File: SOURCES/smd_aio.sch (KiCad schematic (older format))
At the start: 43 parts, among them P2 CONN_01X03, P3 CONN_02X05, Q1 BSS123, Q2 BSS123, Q3 BSS123, Q4 BSS123, Q5 FZT751TA, SW1 SW_PUSH, U2 24AA256SN

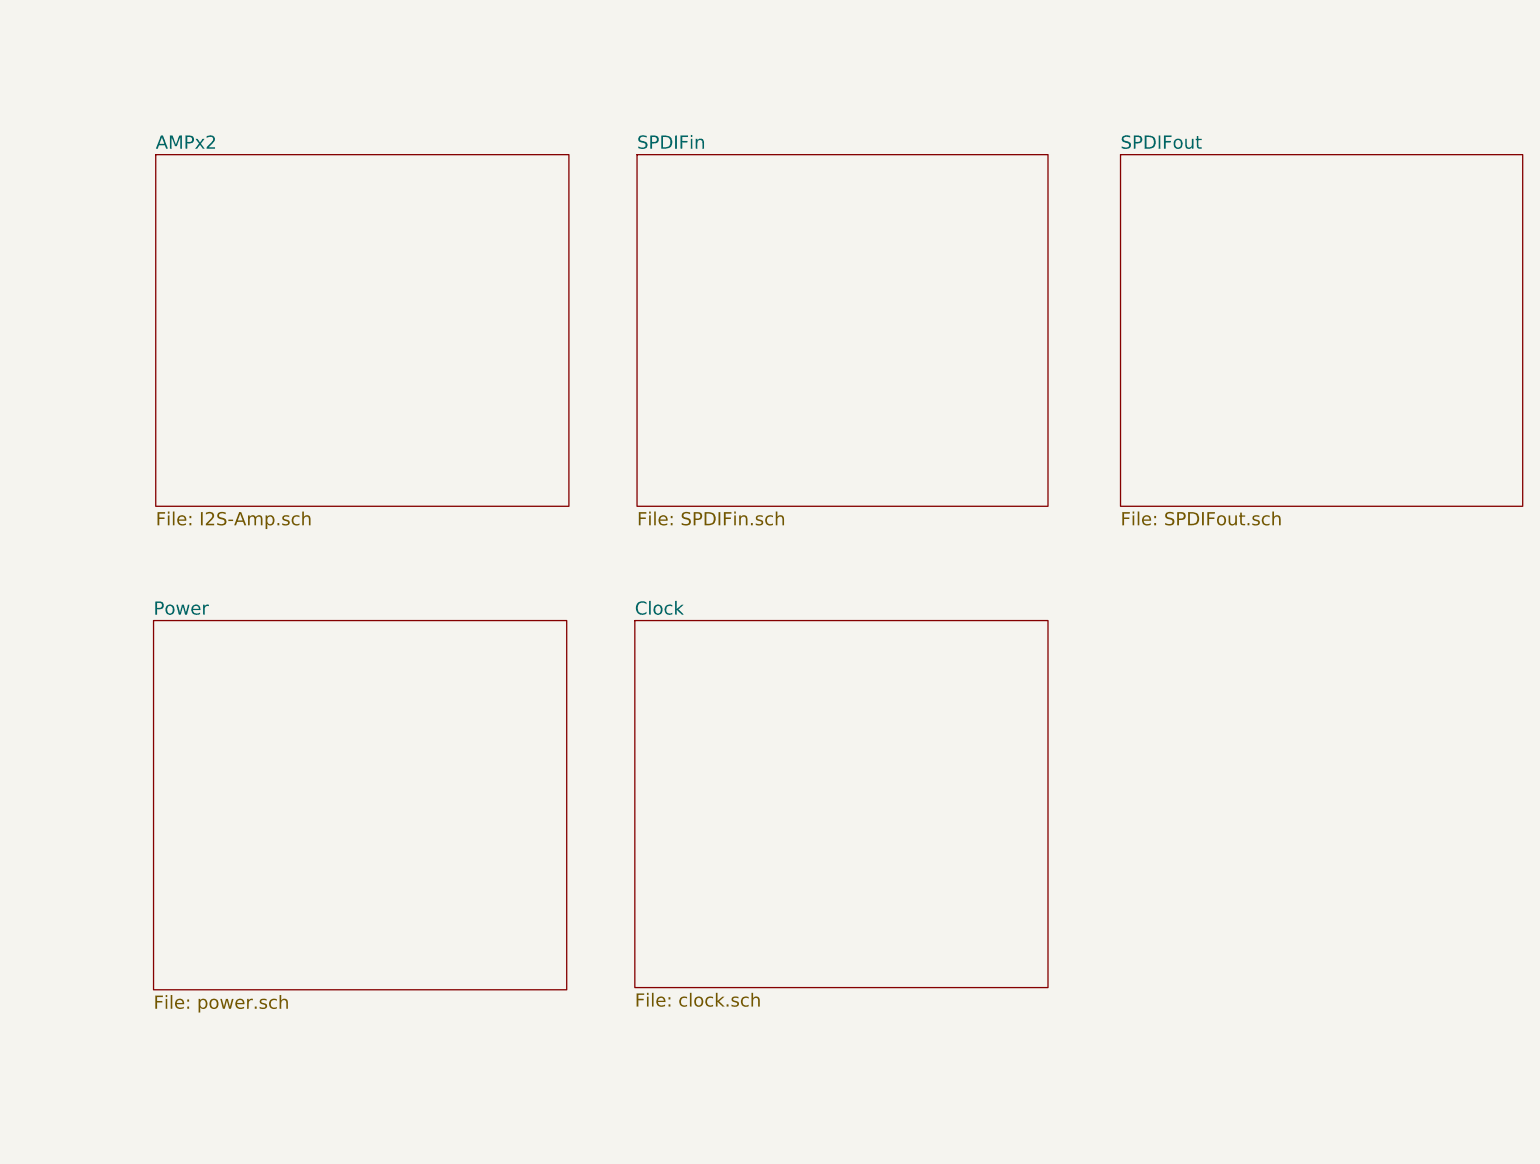
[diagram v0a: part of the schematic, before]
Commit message: adding AMPx2 done
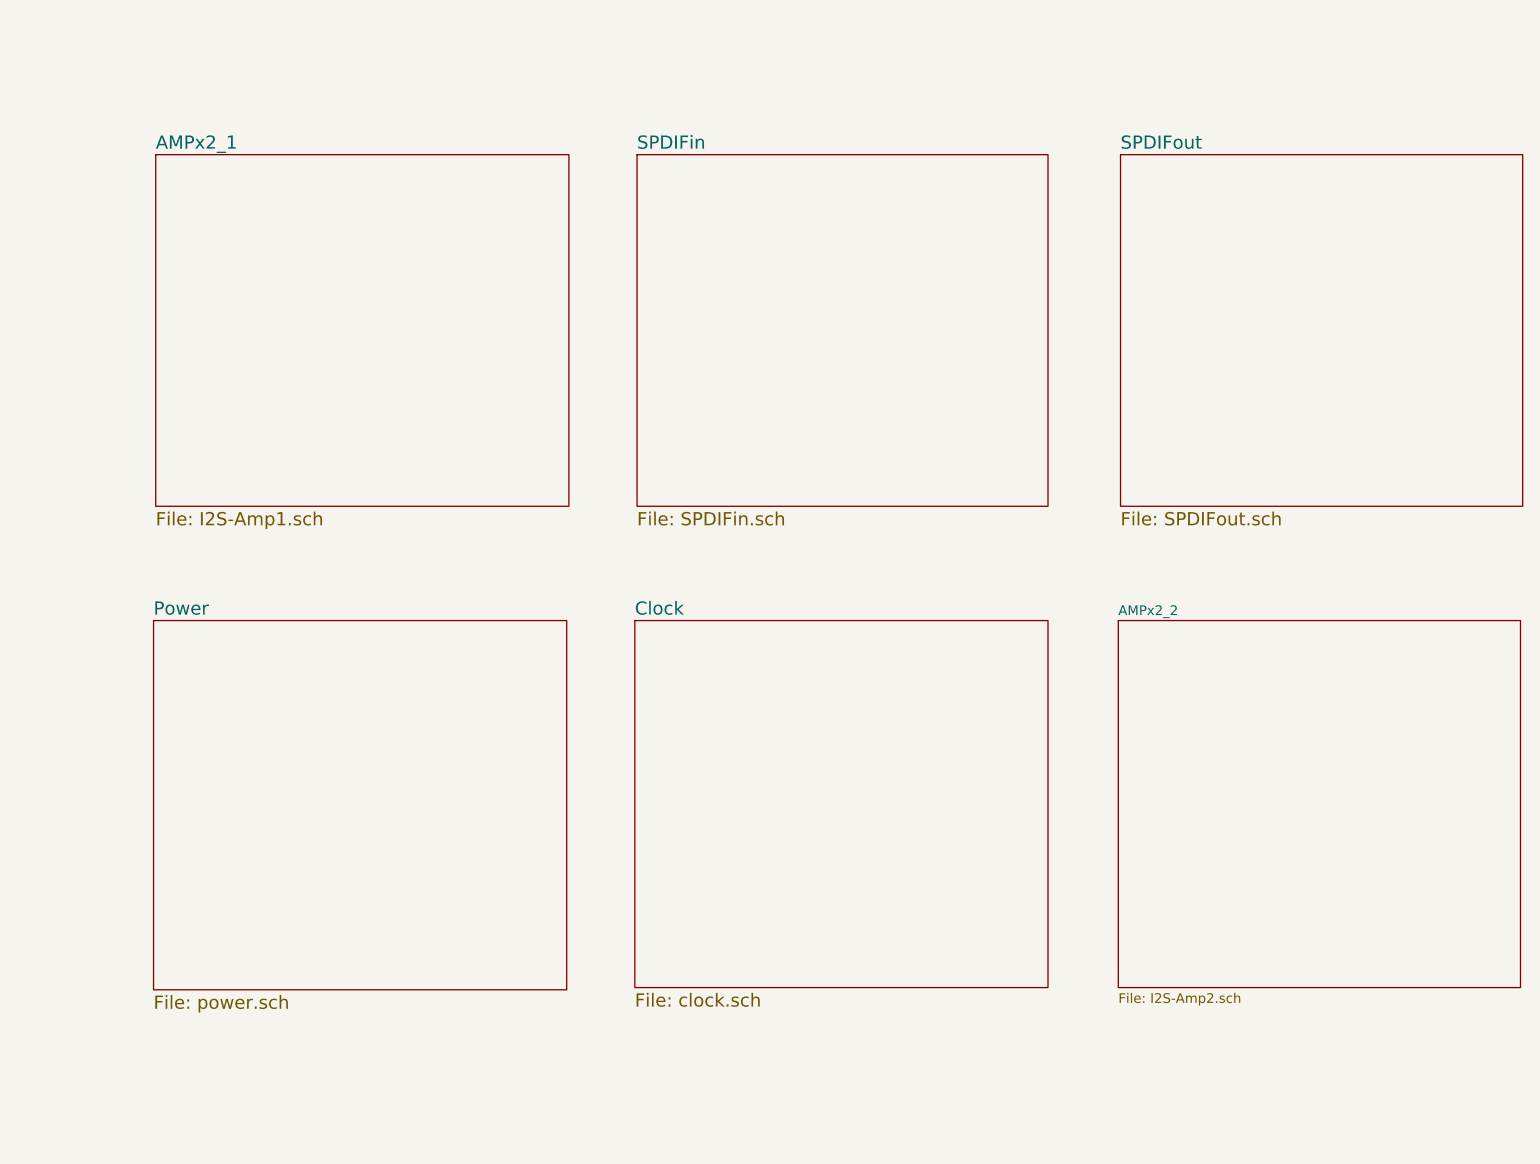
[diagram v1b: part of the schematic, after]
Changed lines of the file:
@@
 $Descr A3 16535 11693
 encoding utf-8
-Sheet 1 6
+Sheet 1 7
 Title ""
 Date ""
@@
 S 9380 1320 1880 1600
 U 5AF9FF80
-F0 "AMPx2" 60
-F1 "I2S-Amp.sch" 60
+F0 "AMPx2_1" 60
+F1 "I2S-Amp1.sch" 60
 $EndSheet
 $Sheet
@@
 F1 "clock.sch" 60
 $EndSheet
+$Sheet
+S 13760 3440 1830 1670
+U 5B04B659
+F0 "AMPx2_2" 44
+F1 "I2S-Amp2.sch" 44
+$EndSheet
 $EndSCHEMATC

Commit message: rearranged sheets
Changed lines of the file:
@@
 	4010 4540 4010 4465
 Wire Wire Line
-	3370 4540 4380 4540
+	3370 4540 3520 4540
+Wire Wire Line
+	3520 4540 3670 4540
+Wire Wire Line
+	3670 4540 3810 4540
+Wire Wire Line
+	3810 4540 4010 4540
+Wire Wire Line
+	4010 4540 4160 4540
+Wire Wire Line
+	4160 4540 4380 4540
 Wire Wire Line
 	3370 4470 3370 4540
@@
 	2720 4300 2720 4210
 Wire Wire Line
-	1440 3900 1440 4250
-Wire Wire Line
-	1420 4110 2720 4110
+	1440 3900 1440 4110
+Wire Wire Line
+	1440 4110 1440 4250
+Wire Wire Line
+	1420 4110 1440 4110
+Wire Wire Line
+	1440 4110 1840 4110
+Wire Wire Line
+	1840 4110 2720 4110
 Connection ~ 1440 4110
 Wire Wire Line
@@
 	740  4110 740  4550
 Wire Wire Line
-	740  4550 1440 4550
+	740  4550 1110 4550
+Wire Wire Line
+	1110 4550 1440 4550
 Wire Wire Line
 	1110 4550 1110 4590
@@
 	3090 1200 2890 1200
 Wire Wire Line
-	2890 1200 2890 1860
+	2890 1200 2890 1470
+Wire Wire Line
+	2890 1470 2890 1750
+Wire Wire Line
+	2890 1750 2890 1860
 Wire Wire Line
 	3090 1470 2890 1470
@@
 	3390 1200 3640 1200
 Wire Wire Line
-	3520 1050 3520 2010
+	3520 1050 3520 2000
+Wire Wire Line
+	3520 2000 3520 2010
 Wire Wire Line
 	3420 2000 3520 2000
@@
 	3610 2010 3610 1860
 Wire Wire Line
-	3610 1860 4080 1860
+	3610 1860 3840 1860
+Wire Wire Line
+	3840 1860 4080 1860
 Wire Wire Line
 	4080 1860 4080 1850
@@
 Connection ~ 3840 1860
 Wire Wire Line
-	4410 1200 4410 1940
+	4410 1200 4410 1300
+Wire Wire Line
+	4410 1300 4410 1570
+Wire Wire Line
+	4410 1570 4410 1940
 Wire Wire Line
 	4410 1570 4420 1570
@@
 Connection ~ 4720 1570
 Wire Wire Line
-	4720 1300 4720 1750
+	4720 1300 4720 1570
+Wire Wire Line
+	4720 1570 4720 1750
 Wire Wire Line
 	4080 1010 4080 1550
@@
 Connection ~ 4410 1570
 Wire Wire Line
-	5010 2010 5010 1030
+	5010 2010 5010 1900
+Wire Wire Line
+	5010 1900 5010 1660
+Wire Wire Line
+	5010 1660 5010 1420
+Wire Wire Line
+	5010 1420 5010 1140
+Wire Wire Line
+	5010 1140 5010 1030
 Wire Wire Line
 	5010 1140 5090 1140
 Wire Wire Line
-	4430 2010 5010 2010
+	4430 2010 4520 2010
+Wire Wire Line
+	4520 2010 4620 2010
+Wire Wire Line
+	4620 2010 5010 2010
 Connection ~ 5010 1140
 Connection ~ 4620 2010
@@
 	5390 1140 5470 1140
 Wire Wire Line
-	5470 1140 5470 2010
+	5470 1140 5470 1420
+Wire Wire Line
+	5470 1420 5470 1660
+Wire Wire Line
+	5470 1660 5470 1900
+Wire Wire Line
+	5470 1900 5470 2010
 Wire Wire Line
 	5390 1900 5470 1900
@@
 	5300 2520 5200 2520
 Wire Wire Line
-	7360 1920 7360 2050
+	7360 1920 7360 2030
+Wire Wire Line
+	7360 2030 7360 2050
 Wire Wire Line
 	7360 2350 7360 2470
@@
 Connection ~ 7360 2030
 Wire Wire Line
-	5200 2820 7360 2820
+	5200 2820 6980 2820
+Wire Wire Line
+	6980 2820 7360 2820
 Wire Wire Line
 	7360 2820 7360 2770
@@
 Connection ~ 6980 2820
 Wire Wire Line
-	5200 2920 6490 2920
+	5200 2920 6190 2920
+Wire Wire Line
+	6190 2920 6490 2920
 Wire Wire Line
 	6490 2920 6490 2970
@@
 Connection ~ 6190 2920
 Wire Wire Line
-	5200 3120 5630 3120
+	5200 3120 5330 3120
+Wire Wire Line
+	5330 3120 5630 3120
 Wire Wire Line
 	5630 3120 5630 3100
@@
 	6190 3270 6190 3340
 Wire Wire Line
-	6190 3340 6490 3340
+	6190 3340 6330 3340
+Wire Wire Line
+	6330 3340 6490 3340
 Wire Wire Line
 	6490 3340 6490 3270
@@
 	5200 3570 5300 3570
 Wire Wire Line
-	5200 3820 5990 3820
+	5200 3820 5660 3820
+Wire Wire Line
+	5660 3820 5990 3820
 Wire Wire Line
 	5660 3820 5660 3880
@@
 Connection ~ 5660 3820
 Wire Wire Line
-	5200 3720 6790 3720
+	5200 3720 6460 3720
+Wire Wire Line
+	6460 3720 6790 3720
 Wire Wire Line
 	6460 3720 6460 3740
@@
 	5660 4180 5660 4220
 Wire Wire Line
-	5660 4220 5990 4220
+	5660 4220 5830 4220
+Wire Wire Line
+	5830 4220 5990 4220
 Wire Wire Line
 	5990 4220 5990 4180
@@
 	6460 4040 6460 4090
 Wire Wire Line
-	6460 4090 6790 4090
+	6460 4090 6620 4090
+Wire Wire Line
+	6620 4090 6790 4090
 Wire Wire Line
 	6790 4090 6790 4040
@@
 	3200 6910 3200 7010
 Wire Wire Line
-	2730 6410 3340 6410
+	2730 6410 2910 6410
+Wire Wire Line
+	2910 6410 3160 6410
+Wire Wire Line
+	3160 6410 3340 6410
 Wire Wire Line
 	3160 5900 3160 6110
@@
 Connection ~ 2910 6410
 Wire Wire Line
-	2430 5770 2430 6130
+	2430 5770 2430 5960
+Wire Wire Line
+	2430 5960 2430 6130
 Wire Wire Line
 	1990 6240 1990 5960
@@
 Connection ~ 2430 5960
 Wire Wire Line
-	2190 6510 3340 6510
+	2190 6510 2430 6510
+Wire Wire Line
+	2430 6510 3340 6510
 Wire Wire Line
 	1620 6510 1790 6510
@@
 	2660 6610 2660 7420
 Wire Wire Line
-	2660 7420 2200 7420
+	2660 7420 2440 7420
+Wire Wire Line
+	2440 7420 2200 7420
 Wire Wire Line
 	2440 7320 2440 7420
 Connection ~ 2440 7420
 Wire Wire Line
-	2440 6840 2440 7020
+	2440 6840 2440 6910
+Wire Wire Line
+	2440 6910 2440 7020
 Wire Wire Line
 	2000 7120 2000 6910
@@
 	1570 8310 1800 8310
 Wire Wire Line
-	2200 8310 2750 8310
+	2200 8310 2420 8310
+Wire Wire Line
+	2420 8310 2750 8310
 Connection ~ 2420 8310
 Wire Wire Line
@@
 	2420 8310 2420 8210
 Wire Wire Line
-	2420 7910 2420 7760
+	2420 7910 2420 7830
+Wire Wire Line
+	2420 7830 2420 7760
 Wire Wire Line
 	2750 8310 2750 6710
@@
 	2750 6710 3340 6710
 Wire Wire Line
-	2200 9090 2850 9090
-Wire Wire Line
-	2420 8540 2420 8690
+	2200 9090 2420 9090
+Wire Wire Line
+	2420 9090 2850 9090
+Wire Wire Line
+	2420 8540 2420 8590
+Wire Wire Line
+	2420 8590 2420 8690
 Wire Wire Line
 	2000 8790 2000 8590
@@
 Connection ~ 2420 9090
 Wire Wire Line
-	5410 5680 5970 5680
+	5410 5680 5640 5680
+Wire Wire Line
+	5640 5680 5970 5680
 Connection ~ 5640 5680
 Wire Wire Line
@@
 	5640 5340 5640 5380
 Wire Wire Line
-	4760 7240 5130 7240
+	4760 7240 4940 7240
+Wire Wire Line
+	4940 7240 5130 7240
 Wire Wire Line
 	4940 7040 4940 7240
@@
 Connection ~ 6950 7640
 Wire Wire Line
-	6950 7330 6950 7200
-Wire Wire Line
-	6620 7740 7660 7740
+	6950 7330 6950 7240
+Wire Wire Line
+	6950 7240 6950 7200
+Wire Wire Line
+	6620 7740 7520 7740
+Wire Wire Line
+	7520 7740 7660 7740
 Wire Wire Line
 	7520 7740 7520 7640
@@
 Connection ~ 6950 7240
 Wire Wire Line
-	5920 8040 5920 8120
+	5920 8040 5920 8060
+Wire Wire Line
+	5920 8060 5920 8120
 Wire Wire Line
 	4760 7340 5460 7340
@@
 	6620 6740 6620 7440
 Wire Wire Line
-	5920 7020 5920 7140
+	5920 7020 5920 7060
+Wire Wire Line
+	5920 7060 5920 7140
 Wire Wire Line
 	6120 7060 5920 7060
 Connection ~ 5920 7060
 Wire Wire Line
-	4760 7440 5220 7440
-Wire Wire Line
-	5070 7440 5070 8060
+	4760 7440 5070 7440
+Wire Wire Line
+	5070 7440 5220 7440
+Wire Wire Line
+	5070 7440 5070 7540
+Wire Wire Line
+	5070 7540 5070 7640
+Wire Wire Line
+	5070 7640 5070 8060
 Wire Wire Line
 	5070 7540 5220 7540
@@
 Connection ~ 5070 7640
 Wire Wire Line
-	6620 7640 7100 7640
+	6620 7640 6950 7640
+Wire Wire Line
+	6950 7640 7100 7640
 Text Notes 5660 6660 0    114  ~ 23
 EEPROM
@@
 $EndSheet
 $Sheet
-S 11570 1320 1870 1600
+S 13780 3470 1820 1650
 U 5AFACECD
 F0 "SPDIFin" 60
@@
 $EndSheet
 $Sheet
-S 11560 3440 1880 1670
+S 11610 1310 1830 1610
+U 5B04B659
+F0 "AMPx2_2" 44
+F1 "I2S-Amp2.sch" 44
+$EndSheet
+$Sheet
+S 11600 3450 1840 1670
 U 5AFACF57
 F0 "Clock" 60
 F1 "clock.sch" 60
 $EndSheet
-$Sheet
-S 13760 3440 1830 1670
-U 5B04B659
-F0 "AMPx2_2" 44
-F1 "I2S-Amp2.sch" 44
-$EndSheet
 $EndSCHEMATC

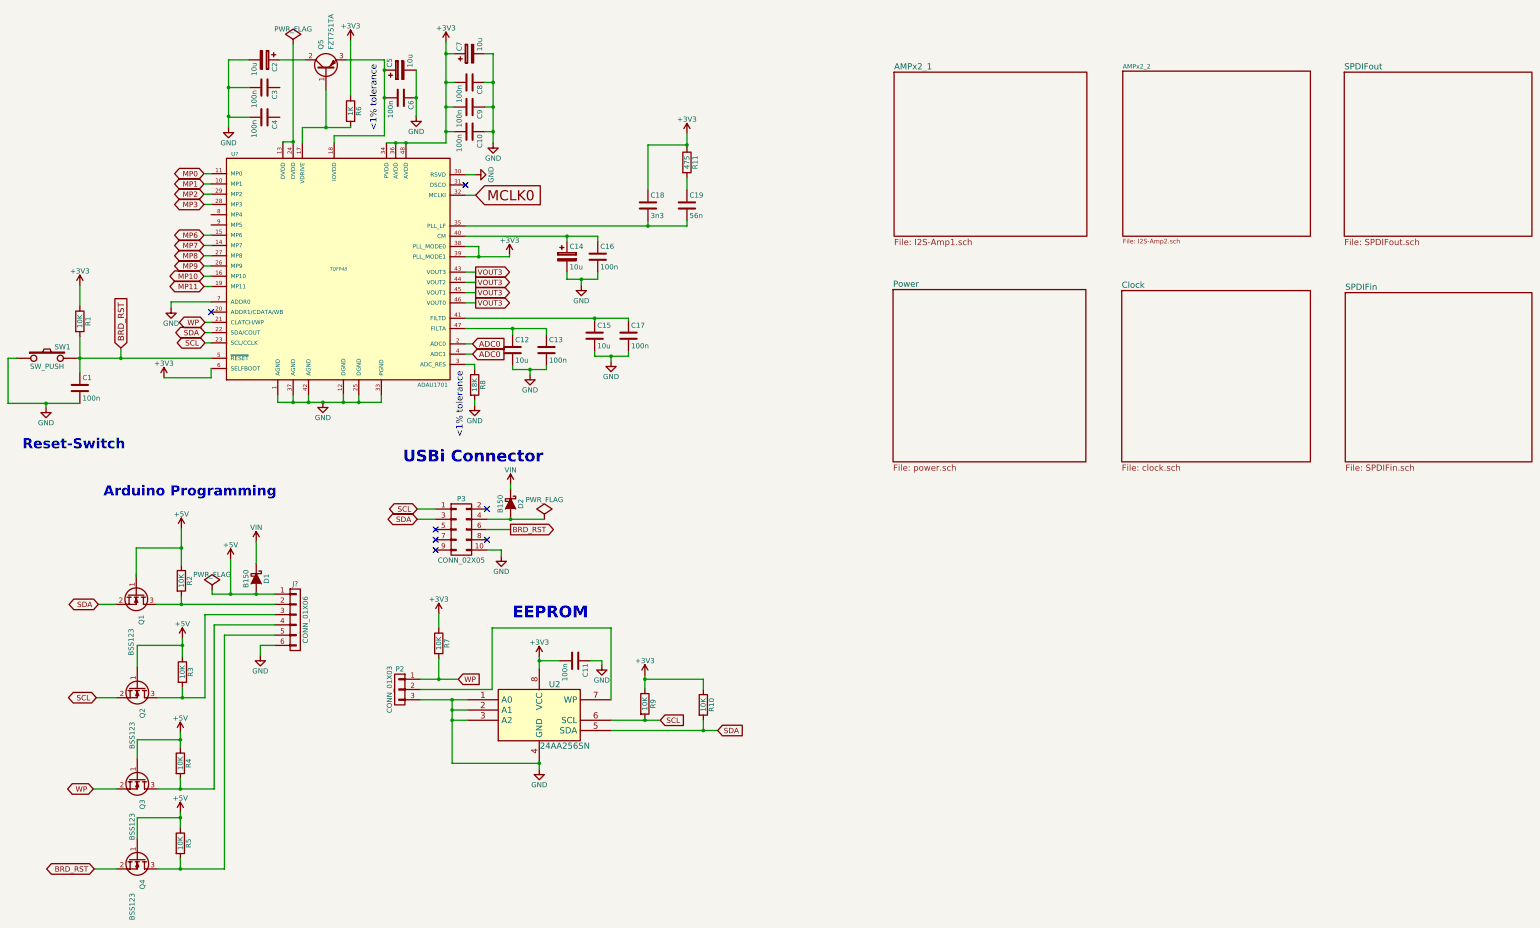
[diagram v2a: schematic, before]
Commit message: added I2S interface
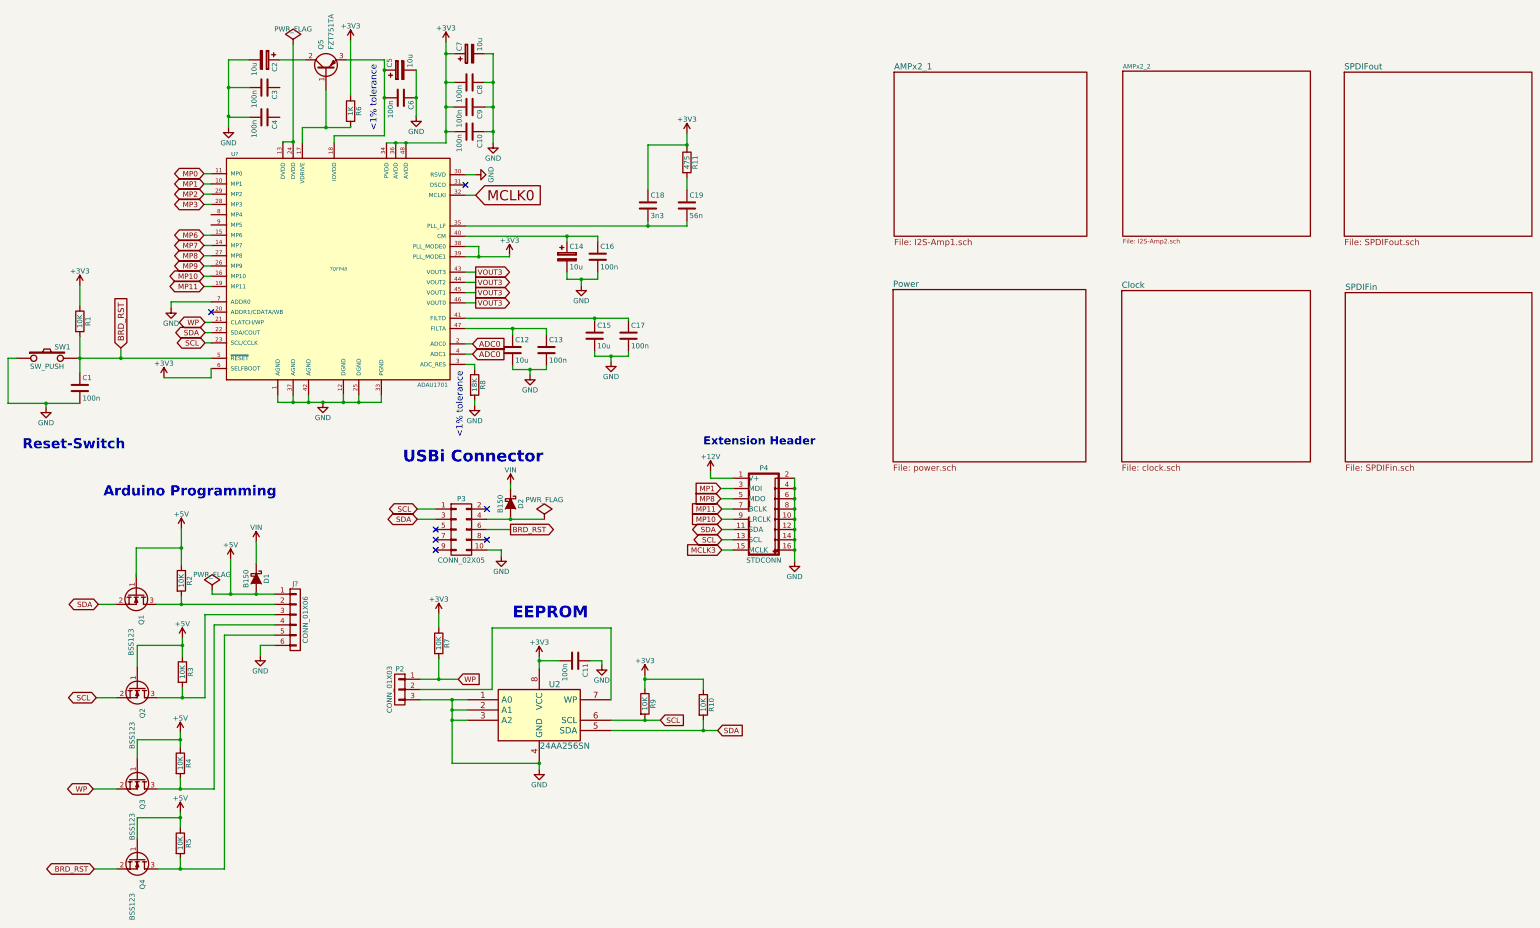
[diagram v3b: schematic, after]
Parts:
- added P4: STDCONN, fdsp_connector:IDC_Header_Straight_16pins, symbol STDCONN
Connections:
- net GND: now also P4.10 (GND), P4.12 (GND), P4.14 (GND), P4.16 (GND), P4.2 (GND), P4.4 (GND), P4.6 (GND), P4.8 (GND)
- net MP1: now also P4.3 (MDI)
- net MP10: now also P4.9 (LRCLK)
- net MP11: now also P4.7 (BCLK)
- net MP8: now also P4.5 (MDO)
- net SCL: now also P4.13 (SCL)
- net SDA: now also P4.11 (SDA)
- new net +12V: P4.1 (V+)
- new net MCLK3: P4.15 (MCLK)
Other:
- note added: "Extension Header"
